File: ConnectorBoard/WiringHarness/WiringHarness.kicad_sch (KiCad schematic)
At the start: 29 parts, among them J1 Barrel_Jack, J2 Conn_01x03, J3 Conn_01x03, J4 Conn_02x05_Odd_Even, J5 Socket, J6 Qwiic, J7 Header, U2 TLV75533PDBV, U3 NCP1117-ADJ_SOT223

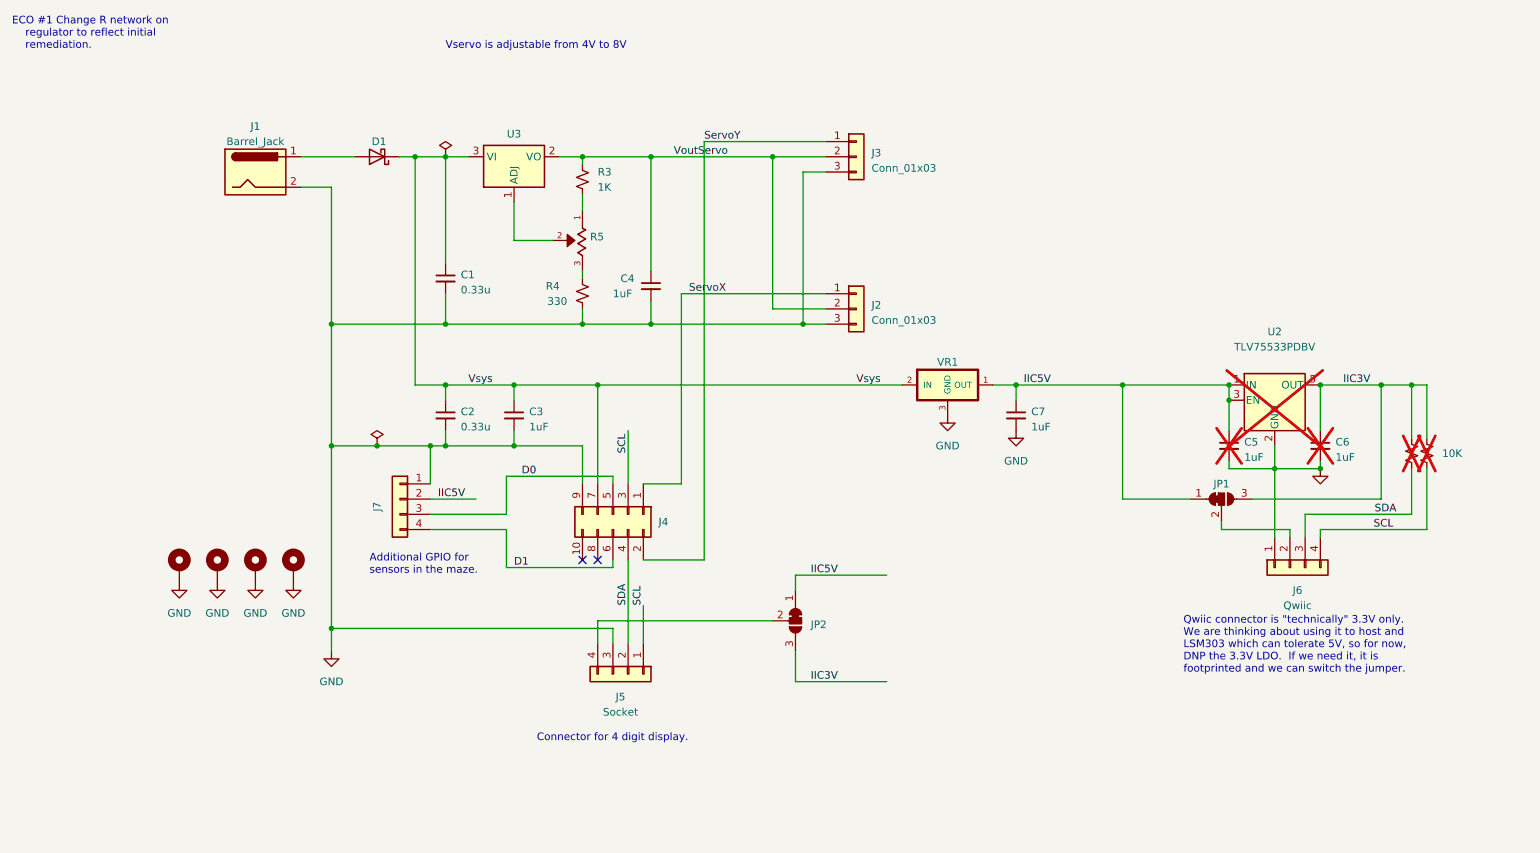
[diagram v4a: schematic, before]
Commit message: Work on #10.
Need to decide if the leadless package is easier to deal with than a small BGA.

Not obvious it is.
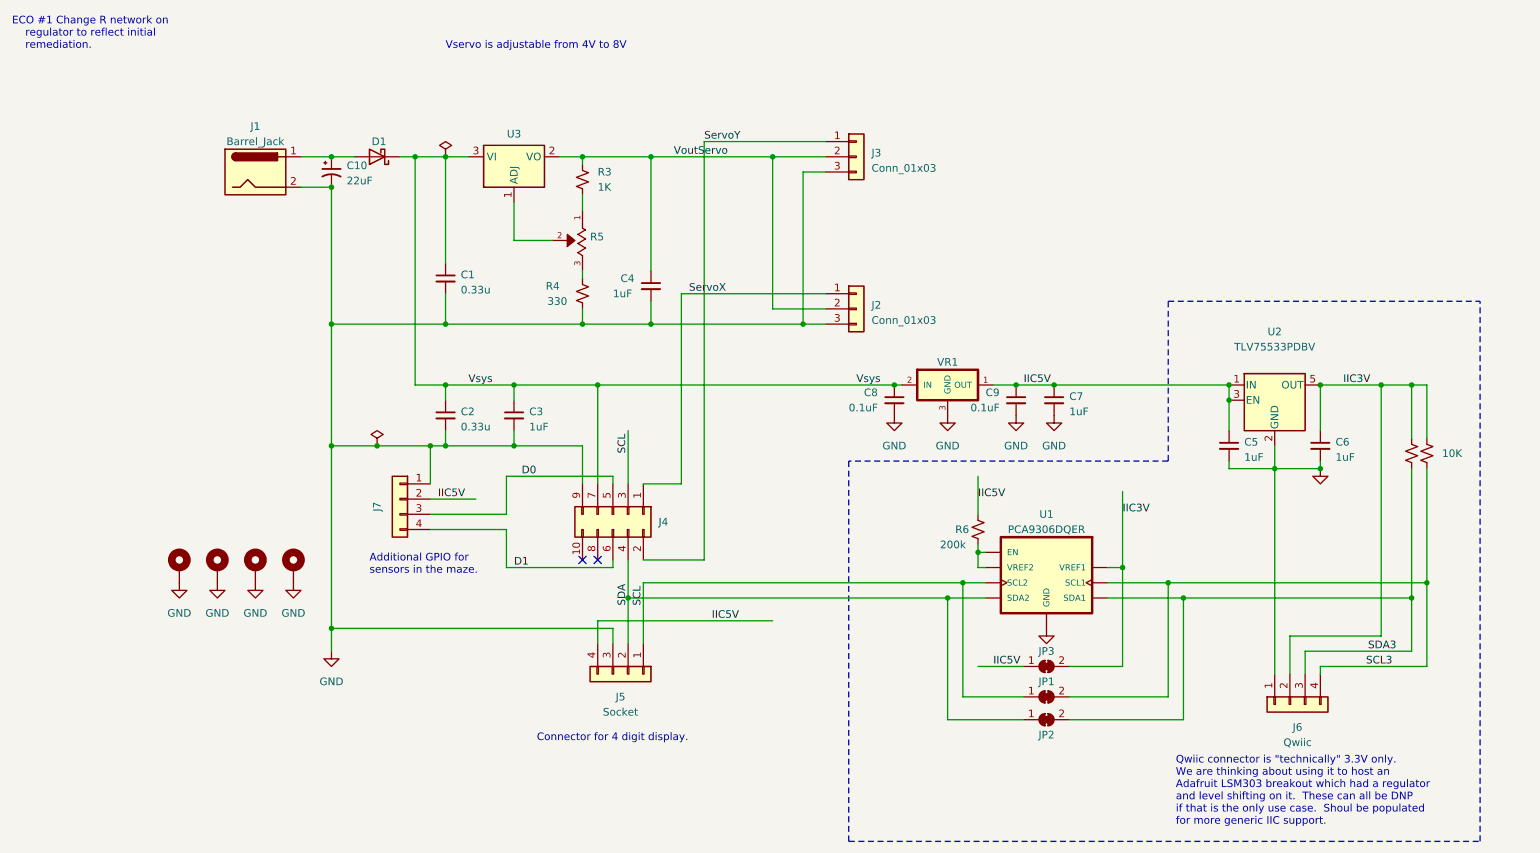
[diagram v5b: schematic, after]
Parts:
- removed JP1, JP2: SolderJumper_3_Bridged12, Jumper:SolderJumper-3_P1.3mm_Bridged12_RoundedPad1.0x1.5mm, symbol Jumper:SolderJumper_3_Bridged12
- added C10: 22uF, Capacitor_THT:CP_Radial_D6.3mm_P2.50mm, symbol Device:C_Polarized_Small_US
- added C8, C9: 0.1uF, Capacitor_SMD:C_0603_1608Metric, symbol Device:C_Small
- added JP1, JP2, JP3: SolderJumper_2_Bridged, Jumper:SolderJumper-2_P1.3mm_Bridged_RoundedPad1.0x1.5mm, symbol Jumper:SolderJumper_2_Bridged
- added R6: 200k, Resistor_SMD:R_0603_1608Metric, symbol Device:R_Small_US
- added U1: PCA9306DQER, Package_SON:X2SON-8_1.4x1mm_P0.35mm, symbol StockedComponents:PCA9306DQER
- C5, C6, R1, R2, U2: now fitted
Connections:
- net GND: now also C10.2, C8.2, C9.2, U1.1 (GND)
- net IIC3V: now also J6.2 (Pin_2), JP3.2 (B), U1.2 (VREF1)
- net IIC5V: now also J5.4 (Pin_4), C9.1, JP3.1 (A), R6.1
- net SCL: now also JP1.1 (A), U1.6 (SCL2); no longer J6.4 (Pin_4), R1.2
- net SDA: now also JP2.1 (A), U1.5 (SDA2); no longer J6.3 (Pin_3), R2.2
- net Vsys: now also C8.1
- net at D1.2 (A), J1.1: now also C10.1
- new net: R6.2, U1.7 (VREF2), U1.8 (EN)
- new net SCL3: J6.4 (Pin_4), JP1.2 (B), R1.2, U1.3 (SCL1)
- new net SDA3: J6.3 (Pin_3), JP2.2 (B), R2.2, U1.4 (SDA1)
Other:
- note added: "Qwiic connector is "technically" 3.3V only. We are thinking about using it to host an Adafruit LSM303 breakout which had a regulator and level shifting on it. These can all be DNP if that is the only use case. Shoul be populated for more generic IIC support."
- note removed: "Qwiic connector is "technically" 3.3V only. We are thinking about using it to host and LSM303 which can tolerate 5V, so for now, DNP the 3.3V LDO. If we need it, it is footprinted and we can switch the jumper."
- moved on the sheet: C7, J6

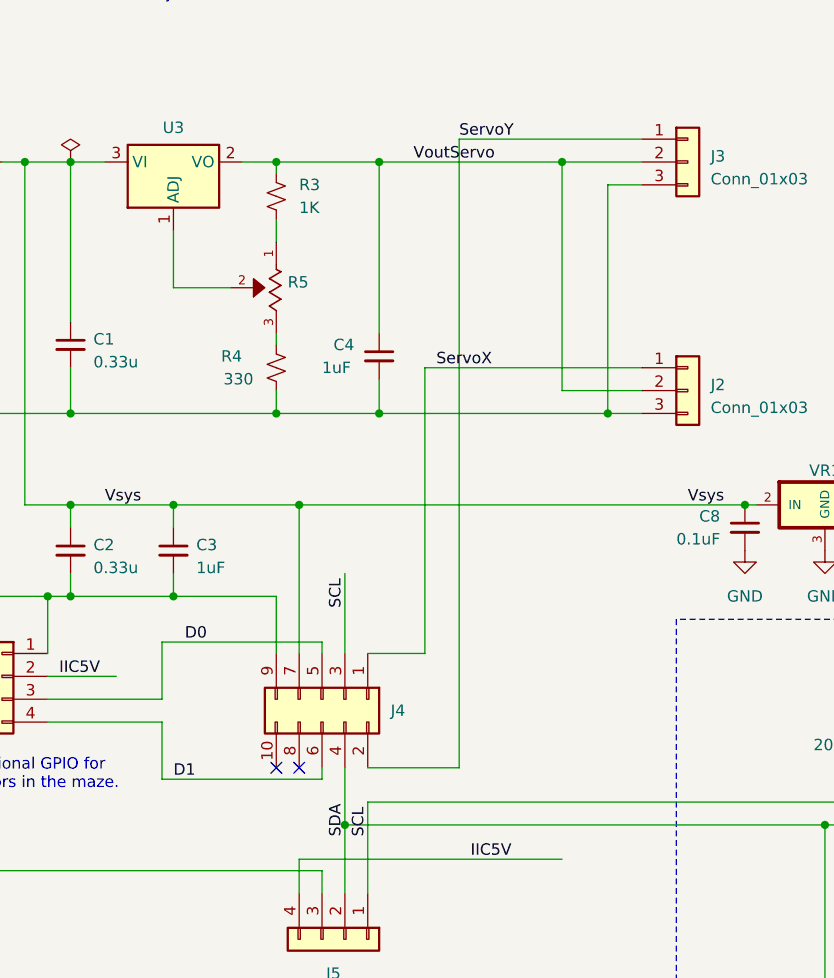
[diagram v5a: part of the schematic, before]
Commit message: signal caps at servo connectors
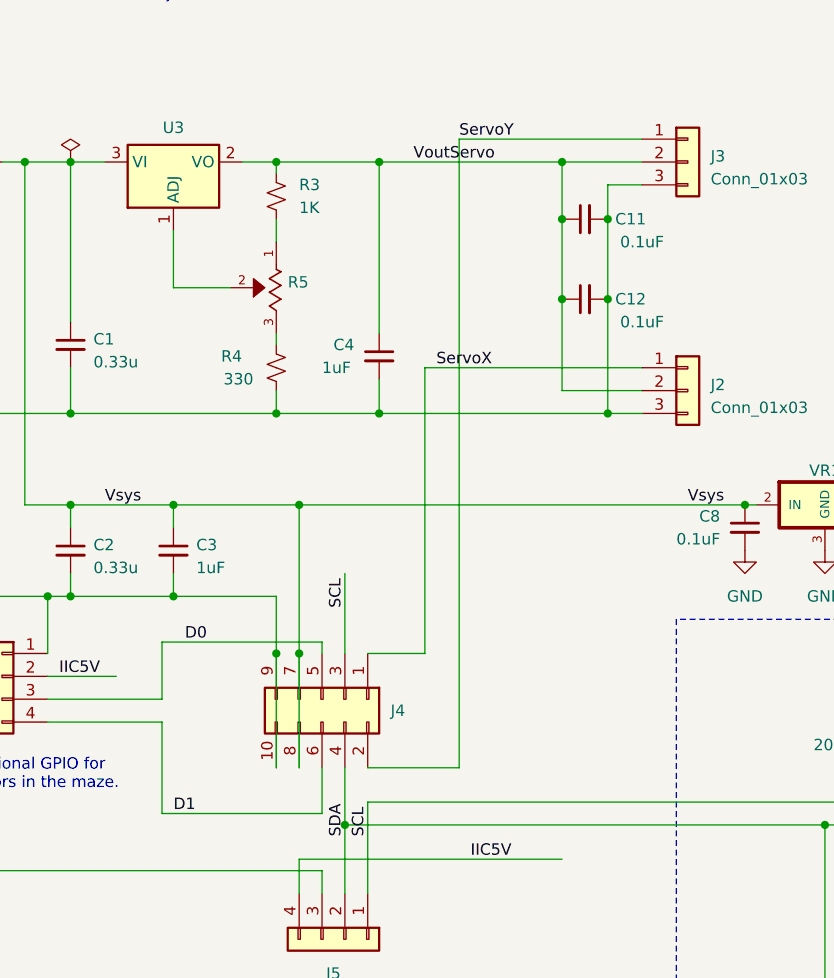
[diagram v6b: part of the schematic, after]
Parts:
- added C11, C12: 0.1uF, Capacitor_SMD:C_0603_1608Metric, symbol Device:C_Small
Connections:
- net GND: now also J4.10 (Pin_10), C11.2, C12.2
- net VoutServo: now also C11.1, C12.1
- net Vsys: now also J4.8 (Pin_8)
- no-connect marks 2 -> 0
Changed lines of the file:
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@@
   (junction (at 128.27 41.91) (diameter 0) (color 0 0 0 0)
   )
+  (junction (at 153.67 57.15) (diameter 0) (color 0 0 0 0)
+  )
   (junction (at 257.81 113.03) (diameter 0) (color 0 0 0 0)
   )
@@
   (junction (at 224.79 82.55) (diameter 0) (color 0 0 0 0)
   )
+  (junction (at 153.67 48.26) (diameter 0) (color 0 0 0 0)
+  )
   (junction (at 168.91 80.01) (diameter 0) (color 0 0 0 0)
   )
+  (junction (at 119.38 96.52) (diameter 0) (color 0 0 0 0)
+  )
   (junction (at 207.01 110.49) (diameter 0) (color 0 0 0 0)
   )
@@
   (junction (at 148.59 41.91) (diameter 0) (color 0 0 0 0)
   )
+  (junction (at 116.84 96.52) (diameter 0) (color 0 0 0 0)
+  )
   (junction (at 88.9 41.91) (diameter 0) (color 0 0 0 0)
   )
@@
   (junction (at 124.46 115.57) (diameter 0) (color 0 0 0 0)
   )
+  (junction (at 148.59 48.26) (diameter 0) (color 0 0 0 0)
+  )
   (junction (at 93.98 41.91) (diameter 0) (color 0 0 0 0)
   )
@@
   (junction (at 93.98 90.17) (diameter 0) (color 0 0 0 0)
   )
-  (no_connect (at 116.84 109.22))
-  (no_connect (at 119.38 109.22))
+  (junction (at 148.59 57.15) (diameter 0) (color 0 0 0 0)
+  )
   (wire (pts (xy 93.98 90.17) (xy 105.41 90.17))
     (stroke (width 0) (type default))
@@
     (stroke (width 0) (type default))
   )
-  (wire (pts (xy 153.67 44.45) (xy 153.67 69.85))
+  (wire (pts (xy 153.67 44.45) (xy 153.67 48.26))
     (stroke (width 0) (type default))
   )
@@
     (stroke (width 0) (type default))
   )
+  (wire (pts (xy 153.67 48.26) (xy 153.67 57.15))
+    (stroke (width 0) (type default))
+  )
   (wire (pts (xy 182.88 107.95) (xy 184.15 107.95))
     (stroke (width 0) (type default))
@@
     (stroke (width 0) (type default))
   )
-  (wire (pts (xy 104.14 110.49) (xy 104.14 104.14))
+  (wire (pts (xy 104.14 114.3) (xy 104.14 104.14))
     (stroke (width 0) (type default))
   )
@@
     (stroke (width 0) (type default))
   )
+  (wire (pts (xy 153.67 57.15) (xy 153.67 69.85))
+    (stroke (width 0) (type default))
+  )
   (wire (pts (xy 224.79 92.71) (xy 224.79 93.98))
     (stroke (width 0) (type default))
   )
+  (wire (pts (xy 148.59 57.15) (xy 148.59 67.31))
+    (stroke (width 0) (type default))
+  )
   (wire (pts (xy 74.93 46.99) (xy 74.93 69.85))
     (stroke (width 0) (type default))
@@
     (stroke (width 0) (type default))
   )
+  (wire (pts (xy 148.59 48.26) (xy 148.59 57.15))
+    (stroke (width 0) (type default))
+  )
   (wire (pts (xy 255.27 115.57) (xy 255.27 124.46))
     (stroke (width 0) (type default))
@@
     (stroke (width 0) (type default))
   )
+  (wire (pts (xy 119.38 96.52) (xy 119.38 109.22))
+    (stroke (width 0) (type default))
+  )
   (wire (pts (xy 133.35 64.77) (xy 133.35 96.52))
     (stroke (width 0) (type default))
@@
     (stroke (width 0) (type default))
   )
-  (wire (pts (xy 121.92 110.49) (xy 104.14 110.49))
+  (wire (pts (xy 121.92 114.3) (xy 104.14 114.3))
     (stroke (width 0) (type default))
   )
@@
     (stroke (width 0) (type default))
   )
-  (wire (pts (xy 148.59 41.91) (xy 148.59 67.31))
+  (wire (pts (xy 148.59 41.91) (xy 148.59 48.26))
     (stroke (width 0) (type default))
   )
@@
     (stroke (width 0) (type default))
   )
+  (wire (pts (xy 116.84 96.52) (xy 116.84 109.22))
+    (stroke (width 0) (type default))
+  )
   (wire (pts (xy 217.17 135.89) (xy 217.17 115.57))
     (stroke (width 0) (type default))
@@
     (stroke (width 0) (type default))
   )
-  (wire (pts (xy 121.92 109.22) (xy 121.92 110.49))
+  (wire (pts (xy 121.92 109.22) (xy 121.92 114.3))
     (stroke (width 0) (type default))
   )
@@
     (effects (font (size 1.27 1.27)) (justify left bottom))
   )
-  (label "D1" (at 105.41 110.49 0) (fields_autoplaced)
+  (label "D1" (at 105.41 114.3 0) (fields_autoplaced)
     (effects (font (size 1.27 1.27)) (justify left bottom))
   )
@@
         (path "/91ed2d93-a6a0-4478-9f77-137103dfe05b"
           (reference "#PWR02") (unit 1)
+        )
+      )
+    )
+  )
+  (symbol (lib_id "Device:C_Small") (at 151.13 57.15 90) (unit 1)
+    (in_bom yes) (on_board yes) (dnp no)
+    (property "Reference" "C12" (at 156.21 57.15 90)
+      (effects (font (size 1.27 1.27)))
+    )
+    (property "Value" "0.1uF" (at 157.48 59.69 90)
+      (effects (font (size 1.27 1.27)))
+    )
+    (property "Footprint" "Capacitor_SMD:C_0603_1608Metric" (at 151.13 57.15 0)
+      (effects (font (size 1.27 1.27)) hide)
+    )
+    (property "Datasheet" "~" (at 151.13 57.15 0)
+      (effects (font (size 1.27 1.27)) hide)
+    )
+    (pin "1")
+    (pin "2")
+    (instances
+      (project "WiringHarness"
+        (path "/91ed2d93-a6a0-4478-9f77-137103dfe05b"
+          (reference "C12") (unit 1)
         )
       )
@@
         )
       )
+    )
+  )
+  (symbol (lib_id "Device:C_Small") (at 151.13 48.26 90) (unit 1)
+    (in_bom yes) (on_board yes) (dnp no)
+    (property "Reference" "C11" (at 156.21 48.26 90)
+      (effects (font (size 1.27 1.27)))
+    )
+    (property "Value" "0.1uF" (at 157.48 50.8 90)
+      (effects (font (size 1.27 1.27)))
+    )
+    (property "Footprint" "Capacitor_SMD:C_0603_1608Metric" (at 151.13 48.26 0)
+      (effects (font (size 1.27 1.27)) hide)
+    )
+    (property "Datasheet" "~" (at 151.13 48.26 0)
+      (effects (font (size 1.27 1.27)) hide)
+    )
+    (pin "1")
+    (pin "2")
+    (instances
+      (project "WiringHarness"
+        (path "/91ed2d93-a6a0-4478-9f77-137103dfe05b"
+          (reference "C11") (unit 1)
+        )
+      )

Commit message: Change footprint for level shifter to something more reasonable.
Add lots of cap to controller.

Add level shifter to controller
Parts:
- U1: footprint Package_SON:X2SON-8_1.4x1mm_P0.35mm -> Package_SO:TSSOP-8_3x3mm_P0.65mm
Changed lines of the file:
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@@
       (effects (font (size 1.27 1.27)))
     )
-    (property "Footprint" "Package_SON:X2SON-8_1.4x1mm_P0.35mm" (at 189.23 110.49 0)
+    (property "Footprint" "Package_SO:TSSOP-8_3x3mm_P0.65mm" (at 189.23 110.49 0)
       (effects (font (size 1.27 1.27)) (justify bottom) hide)
     )

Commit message: Hard to believe, but I had the resistors backward again on the regulator...
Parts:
- R3: value 1K -> 300; Digikey RMCF0603FT100RCT-ND -> RMCF0603FT300RCT-ND; Vendor RMCF0603FT100RCT-ND -> RMCF0603FT300RCT-ND
- R4: value 330 -> 1K; Digikey RMCF0603FT300RCT-ND -> (none); Vendor RMCF0603FT300RCT-ND -> (none)
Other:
- note removed: "ECO #1 Change R network on regulator to reflect initial remediation."
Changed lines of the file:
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@@
-    (effects (font (size 1.27 1.27)) (justify left bottom))
-  )
-  (text "ECO #1 Change R network on \n	regulator to reflect initial \n	remediation."
-    (at 21.59 24.13 0)
     (effects (font (size 1.27 1.27)) (justify left bottom))
   )
@@
       (effects (font (size 1.27 1.27)) (justify left))
     )
-    (property "Value" "1K" (at 119.38 46.99 0)
+    (property "Value" "300" (at 119.38 46.99 0)
       (effects (font (size 1.27 1.27)) (justify left))
     )
@@
       (effects (font (size 1.27 1.27)) hide)
     )
-    (property "Digikey" "RMCF0603FT100RCT-ND" (at 116.84 45.72 0)
-      (effects (font (size 1.27 1.27)) hide)
-    )
-    (property "Vendor" "RMCF0603FT100RCT-ND" (at 116.84 45.72 0)
+    (property "Digikey" "RMCF0603FT300RCT-ND" (at 116.84 45.72 0)
+      (effects (font (size 1.27 1.27)) hide)
+    )
+    (property "Vendor" "RMCF0603FT300RCT-ND" (at 116.84 45.72 0)
       (effects (font (size 1.27 1.27)) hide)
     )
@@
       (effects (font (size 1.27 1.27)) (justify left))
     )
-    (property "Value" "330" (at 114.3 66.04 0)
+    (property "Value" "1K" (at 114.3 66.04 0)
       (effects (font (size 1.27 1.27)) (justify left))
     )
@@
       (effects (font (size 1.27 1.27)) hide)
     )
-    (property "Digikey" "RMCF0603FT300RCT-ND" (at 116.84 64.77 0)
-      (effects (font (size 1.27 1.27)) hide)
-    )
-    (property "Vendor" "RMCF0603FT300RCT-ND" (at 116.84 64.77 0)
-      (effects (font (size 1.27 1.27)) hide)
-    )
+    (property "Digikey" "" (at 116.84 64.77 0)
+      (effects (font (size 1.27 1.27)) hide)
+    )
+    (property "Vendor" "" (at 116.84 64.77 0)
+      (effects (font (size 1.27 1.27)) hide)
+    )
